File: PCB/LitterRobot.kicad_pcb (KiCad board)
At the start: 4 copper layers, 55 x 140 mm, 150 parts, among them J1 DF11C-4DP-2V(57), J2 DF11C-6DP-2V(57), J3 DF11C-8DP-2V(57), J4 DF11C-6DP-2V(57), J5 TSM-105-01-S-DV, Q1 BSS138, Q10 BC817, Q11 BC817, Q12 BC817, Q13 BC817, Q14 BC817, Q15 BC817, Q16 BC817, Q17 BC817, Q18 BC817, Q19 BC817, Q2 BSS138, Q20 BC817, Q21 BC817, Q22 BC817, Q23 BC817, Q24 BC817, Q3 BC817, Q4 BC817, Q5 BC817, Q6 BC817, Q7 BC817, Q8 BC817, Q9 BC817, SW1 PCB_Push_Button, SW2 PCB_Push_Button, SW3 PCB_Push_Button, SW4 PCB_Push_Button, SW5 PCB_Push_Button, SW6 PCB_Push_Button, U1 MPM54304GMN-0001, U2 10CL016YE144C8G, U3 S25FL128SAGMFI000, U4 DRV8871DDA, U5 MCP1700T-5002E/TT, U6 VEML6035, X1 X1G0044510011

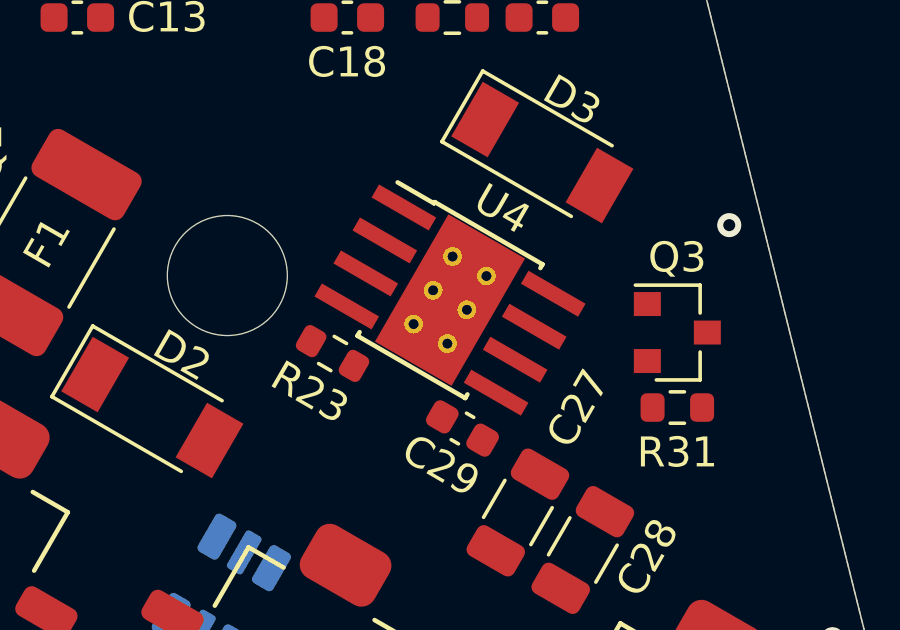
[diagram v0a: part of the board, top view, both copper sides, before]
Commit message: Adapt the DRV8871 footprint for the PCB constraints
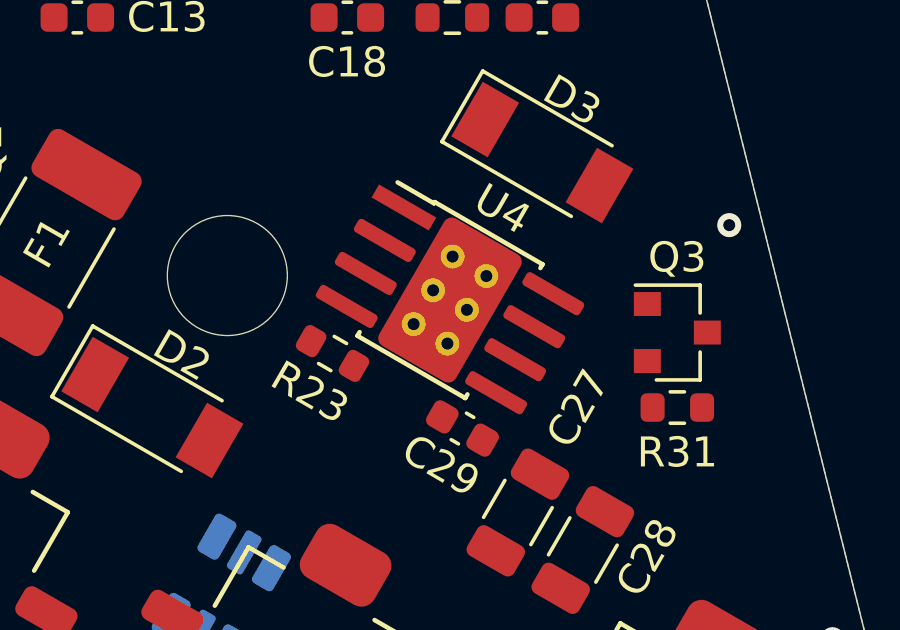
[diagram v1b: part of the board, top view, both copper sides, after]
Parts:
- U4: footprint Package_SO:Texas_HTSOP-8-1EP_3.9x4.9mm_P1.27mm_EP2.95x4.9mm_Mask2.4x3.1mm_ThermalVias -> LitterRobot:Texas_DRV8871
